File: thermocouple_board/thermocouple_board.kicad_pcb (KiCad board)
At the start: 2 copper layers, 152.4 x 140 mm, 13 parts, among them J1 PCIE Card Edge, J2 DSUB1, U1 MAX31856, U2 MAX31856, U3 PCF8575_Breakout, U4 MAX31856, U5 MAX31856, U6 MAX31856

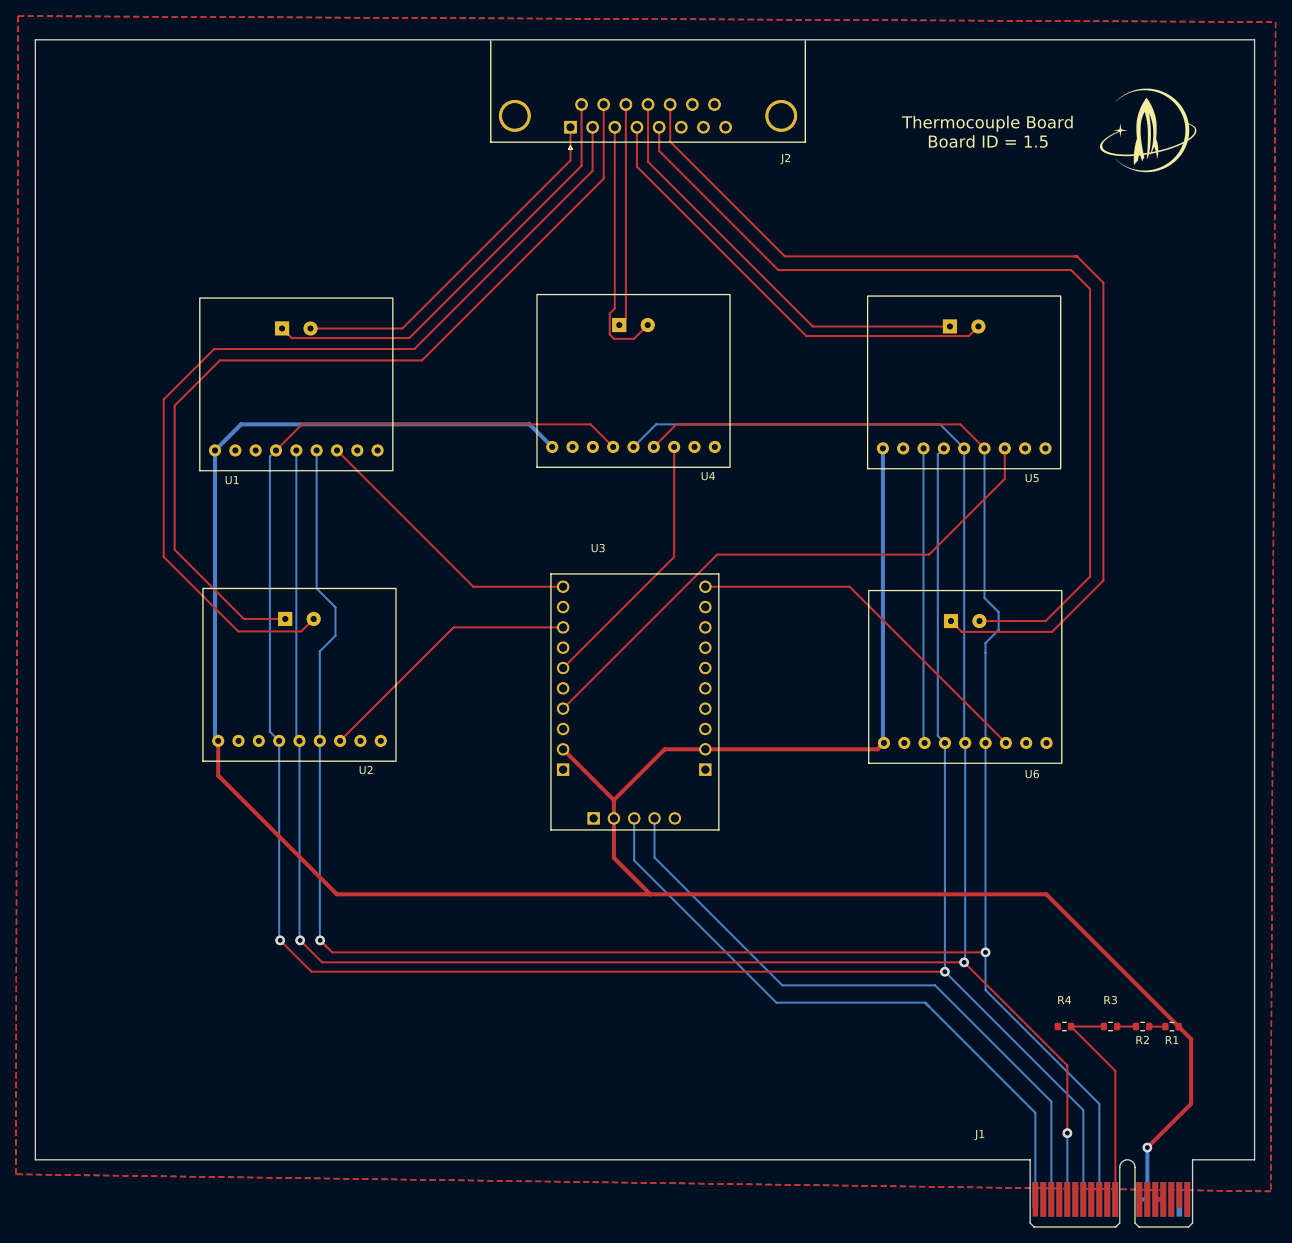
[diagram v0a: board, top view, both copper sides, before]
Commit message: Fixing errors in thermocouple_board.
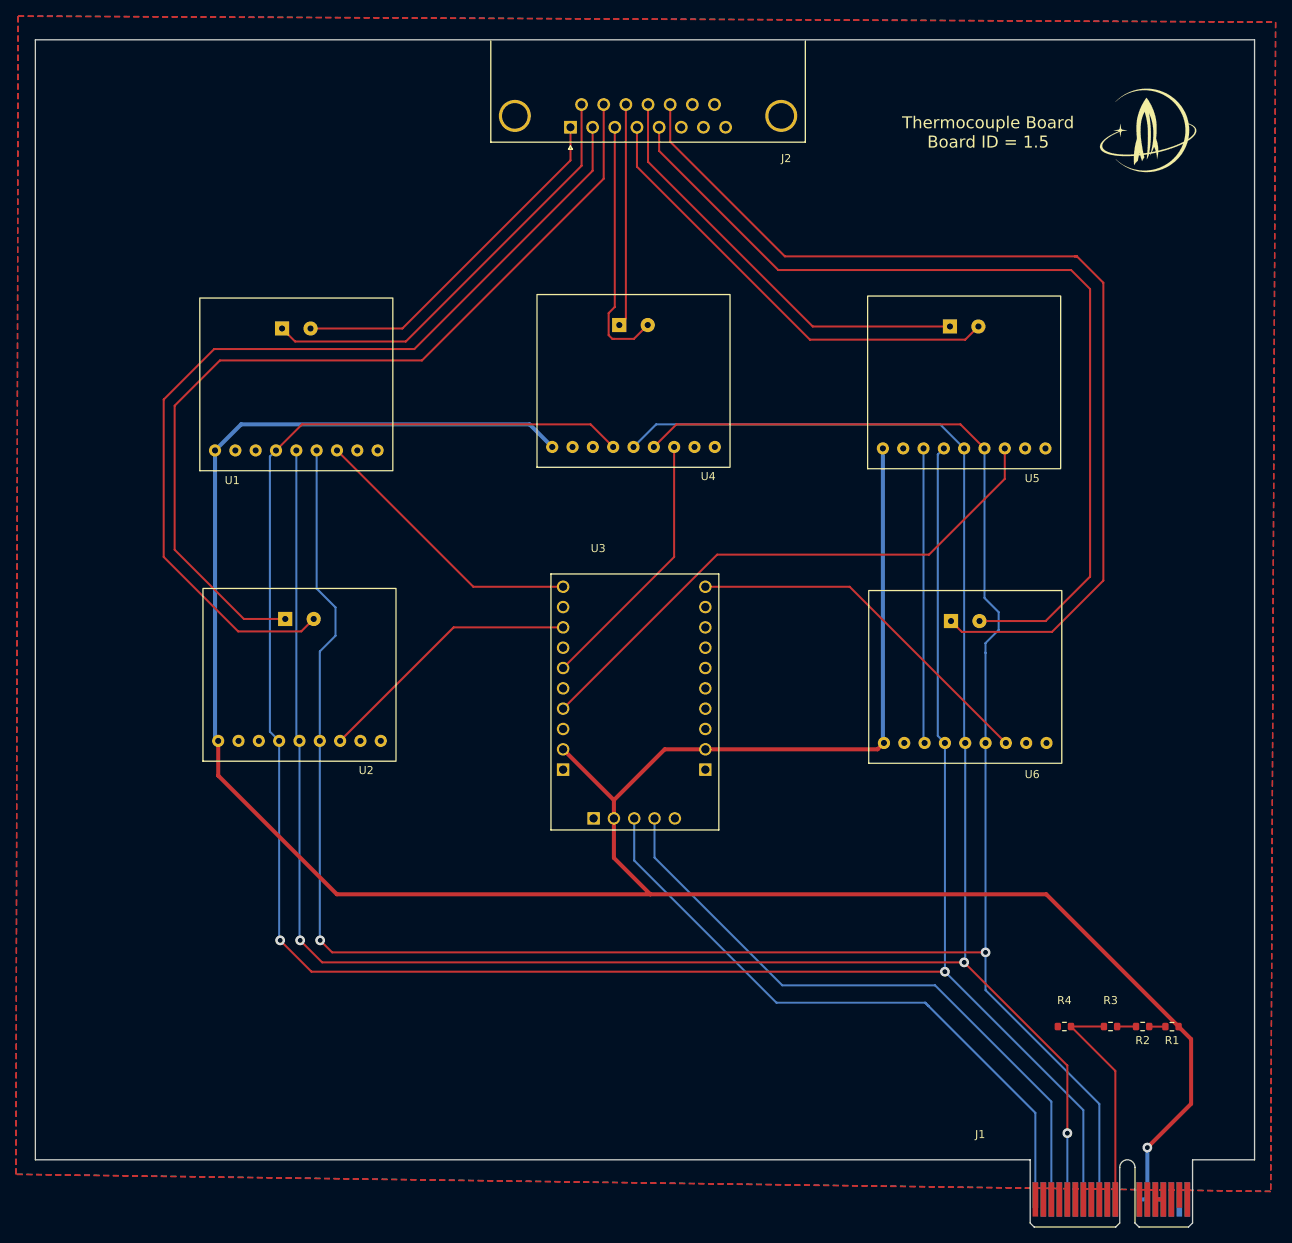
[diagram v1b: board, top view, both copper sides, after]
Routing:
- net /SPI_MOSI: track 293.2 -> 291.8 mm
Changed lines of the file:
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@@
   (segment (start 154.425 141.75) (end 72.75 141.75) (width 0.254) (layer "F.Cu") (net 9))
   (segment (start 72.75 141.75) (end 71.25 140.25) (width 0.254) (layer "F.Cu") (net 9))
-  (segment (start 72.25 141.25) (end 71.25 140.25) (width 0.254) (layer "F.Cu") (net 9))
   (segment (start 151.285 75.75) (end 115.785 75.75) (width 0.254) (layer "F.Cu") (net 9))
   (segment (start 154.29 78.755) (end 151.285 75.75) (width 0.254) (layer "F.Cu") (net 9))
@@
   (segment (start 83.025 66.335) (end 58.005 66.335) (width 0.254) (layer "F.Cu") (net 34))
   (segment (start 110.473 65.06) (end 107.980378 65.06) (width 0.254) (layer "F.Cu") (net 35))
-  (segment (start 107.980378 65.06) (end 107.448689 64.528311) (width 0.254) (layer "F.Cu") (net 35))
+  (segment (start 108.08 61.07) (end 107.31 61.84) (width 0.254) (layer "F.Cu") (net 35))
   (segment (start 112.198 63.335) (end 110.473 65.06) (width 0.254) (layer "F.Cu") (net 35))
-  (segment (start 107.448689 61.891311) (end 108.08 61.26) (width 0.254) (layer "F.Cu") (net 35))
-  (segment (start 108.08 61.26) (end 108.08 38.61) (width 0.254) (layer "F.Cu") (net 35))
-  (segment (start 107.448689 64.528311) (end 107.448689 61.891311) (width 0.254) (layer "F.Cu") (net 35))
+  (segment (start 107.31 64.6) (end 107.77 65.06) (width 0.254) (layer "F.Cu") (net 35))
+  (segment (start 108.08 61.07) (end 108.08 38.61) (width 0.254) (layer "F.Cu") (net 35))
+  (segment (start 107.31 61.84) (end 107.31 64.6) (width 0.254) (layer "F.Cu") (net 35))
+  (segment (start 107.77 65.06) (end 107.980378 65.06) (width 0.254) (layer "F.Cu") (net 35))
+  (segment (start 151.883 65.16) (end 132.47 65.16) (width 0.254) (layer "F.Cu") (net 36))
+  (segment (start 132.47 65.16) (end 110.85 43.54) (width 0.254) (layer "F.Cu") (net 36))
   (segment (start 110.85 43.54) (end 110.85 38.61) (width 0.254) (layer "F.Cu") (net 36))
-  (segment (start 132.018311 64.708311) (end 110.85 43.54) (width 0.254) (layer "F.Cu") (net 36))
-  (segment (start 152.334689 64.708311) (end 132.018311 64.708311) (width 0.254) (layer "F.Cu") (net 36))
-  (segment (start 153.528 63.515) (end 152.334689 64.708311) (width 0.254) (layer "F.Cu") (net 36))
+  (segment (start 153.528 63.515) (end 151.883 65.16) (width 0.254) (layer "F.Cu") (net 36))
   (segment (start 113.62 38.61) (end 113.62 41.57) (width 0.254) (layer "F.Cu") (net 37))
   (segment (start 167.49 58.83) (end 167.49 94.78) (width 0.254) (layer "F.Cu") (net 37))
   (segment (start 167.49 94.78) (end 161.936 100.334) (width 0.254) (layer "F.Cu") (net 37))
-  (segment (start 157.826 100.334) (end 157.394 100.334) (width 0.254) (layer "F.Cu") (net 37))
   (segment (start 128.51 56.46) (end 165.12 56.46) (width 0.254) (layer "F.Cu") (net 37))
   (segment (start 165.12 56.46) (end 167.49 58.83) (width 0.254) (layer "F.Cu") (net 37))
@@
   (segment (start 113.62 41.57) (end 128.51 56.46) (width 0.254) (layer "F.Cu") (net 37))
   (segment (start 157.394 100.334) (end 153.663 100.334) (width 0.254) (layer "F.Cu") (net 37))
+  (segment (start 68.117 65.39) (end 81.96 65.39) (width 0.254) (layer "F.Cu") (net 41))
   (segment (start 103.925 43.425) (end 103.925 35.77) (width 0.254) (layer "F.Cu") (net 41))
-  (segment (start 67.685311 64.958311) (end 82.391689 64.958311) (width 0.254) (layer "F.Cu") (net 41))
-  (segment (start 66.492 63.765) (end 67.685311 64.958311) (width 0.254) (layer "F.Cu") (net 41))
-  (segment (start 82.391689 64.958311) (end 103.925 43.425) (width 0.254) (layer "F.Cu") (net 41))
-  (segment (start 66.887 100.074) (end 66.887 99.887) (width 0.254) (layer "F.Cu") (net 42))
-  (segment (start 83.98 67.76) (end 58.72 67.76) (width 0.254) (layer "F.Cu") (net 42))
-  (segment (start 53.06 91.42) (end 61.714 100.074) (width 0.254) (layer "F.Cu") (net 42))
-  (segment (start 53.06 73.42) (end 53.06 91.42) (width 0.254) (layer "F.Cu") (net 42))
-  (segment (start 58.72 67.76) (end 53.06 73.42) (width 0.254) (layer "F.Cu") (net 42))
-  (segment (start 106.72 45.02) (end 83.98 67.76) (width 0.254) (layer "F.Cu") (net 42))
-  (segment (start 106.695 44.995) (end 106.695 35.77) (width 0.254) (layer "F.Cu") (net 42))
-  (segment (start 61.714 100.074) (end 66.887 100.074) (width 0.254) (layer "F.Cu") (net 42))
+  (segment (start 66.492 63.765) (end 68.117 65.39) (width 0.254) (layer "F.Cu") (net 41))
+  (segment (start 81.96 65.39) (end 103.925 43.425) (width 0.254) (layer "F.Cu") (net 41))
+  (segment (start 58.72 67.76) (end 83.98 67.76) (width 0.254) (layer "F.Cu") (net 42))
+  (segment (start 53.06 91.42) (end 53.06 73.42) (width 0.254) (layer "F.Cu") (net 42))
+  (segment (start 83.98 67.76) (end 106.695 45.045) (width 0.254) (layer "F.Cu") (net 42))
+  (segment (start 106.695 45.045) (end 106.695 35.77) (width 0.254) (layer "F.Cu") (net 42))
+  (segment (start 53.06 73.42) (end 58.72 67.76) (width 0.254) (layer "F.Cu") (net 42))
+  (segment (start 66.887 100.074) (end 61.714 100.074) (width 0.254) (layer "F.Cu") (net 42))
+  (segment (start 61.714 100.074) (end 53.06 91.42) (width 0.254) (layer "F.Cu") (net 42))
   (segment (start 108.642 63.335) (end 109.465 62.512) (width 0.254) (layer "F.Cu") (net 43))
   (segment (start 109.465 62.512) (end 109.465 35.77) (width 0.254) (layer "F.Cu") (net 43))
@@
   (segment (start 151.463 101.69) (end 150.107 100.334) (width 0.254) (layer "F.Cu") (net 45))
   (segment (start 162.73 101.69) (end 151.463 101.69) (width 0.254) (layer "F.Cu") (net 45))
-  (segment (start 115.14 35.77) (end 115.005 35.77) (width 0.254) (layer "F.Cu") (net 45))
   (segment (start 115.005 40.415) (end 129.34 54.75) (width 0.254) (layer "F.Cu") (net 45))
   (segment (start 129.34 54.75) (end 165.58 54.75) (width 0.254) (layer "F.Cu") (net 45))
